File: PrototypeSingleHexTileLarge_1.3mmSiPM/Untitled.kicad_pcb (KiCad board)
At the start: 2 copper layers, 44.6 x 38.6 mm, 7 parts

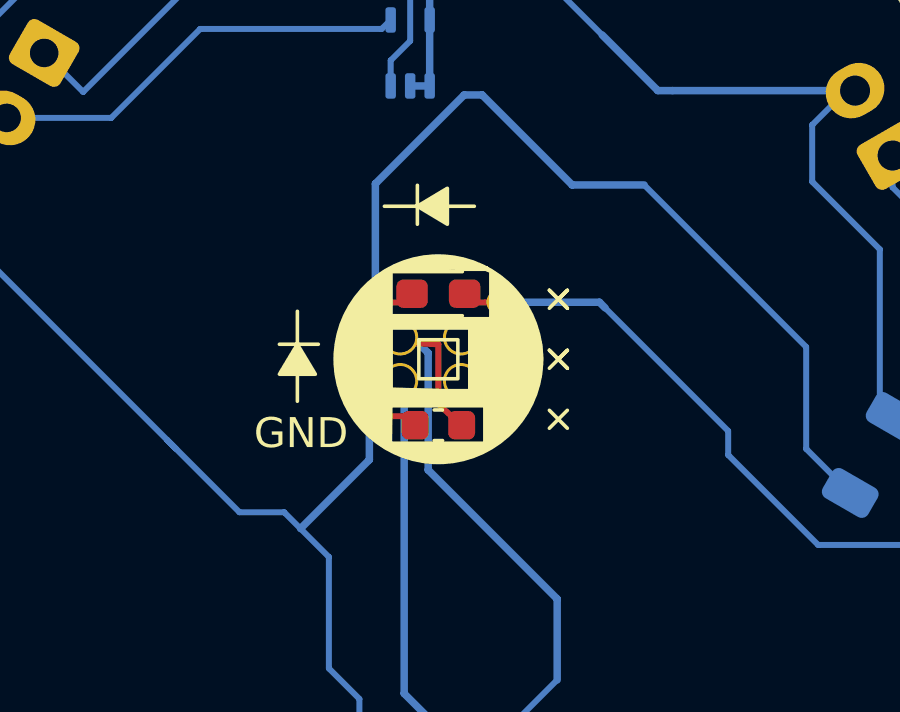
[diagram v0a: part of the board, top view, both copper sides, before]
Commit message: updated 1.3 mm SiPM board (single hex).  Increased size of holes for the pogos
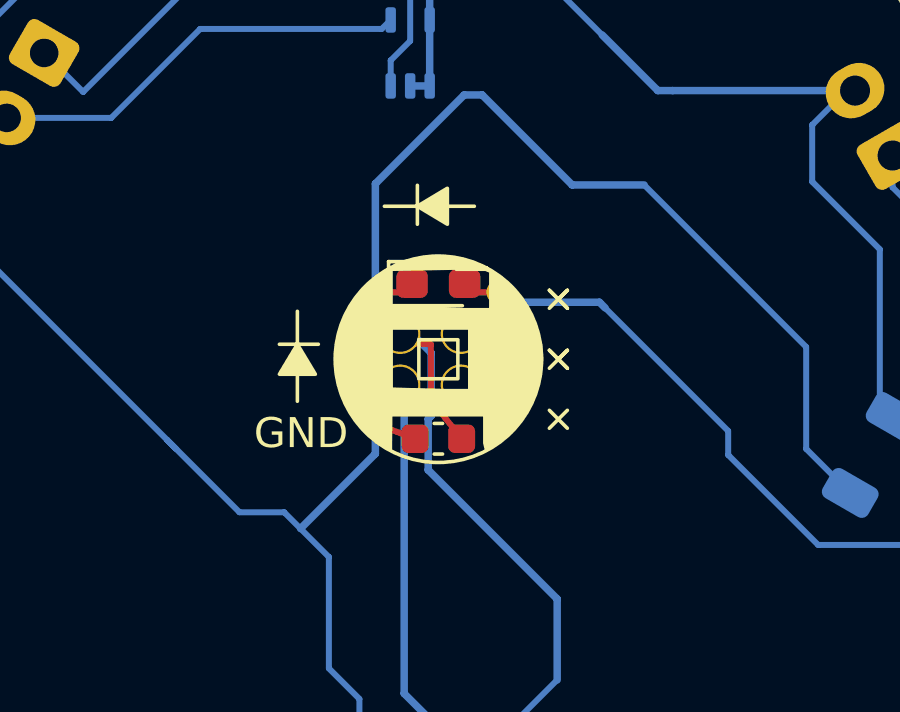
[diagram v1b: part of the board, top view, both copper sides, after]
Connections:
- REF** pad 5: (no net) -> LED_C
- REF** pad 6: (no net) -> LED_A
- REF** pad 7: (no net) -> SiPM_C
- REF** pad 8: (no net) -> SiPM_A
- REF** pad 9: (no net) -> GND
- REF** pad 1: (no net) -> GND (x2)
- REF** pad 2: (no net) -> GND (x2)
- REF** pad 3: (no net) -> TMP_OUT
- REF** pad 4: (no net) -> TMP_VDD
- REF** pad 5: (no net) -> GND
- REF** pad 1: (no net) -> TMP_OUT
- REF** pad 2: (no net) -> TMP_VDD
- REF** pad 3: (no net) -> GND (x2)
- REF** pad 1: (no net) -> SiPM_C
- REF** pad 2: (no net) -> SiPM_A
- REF** pad 2: (no net) -> LED_C
- REF** pad 1: (no net) -> LED_A
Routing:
- net (no net): track 224.4 -> 0.00 mm
- net GND: track 0.00 -> 90.2 mm
- net LED_A: track 0.00 -> 33.4 mm
- net LED_C: track 0.00 -> 28.2 mm
- net SiPM_C: track 0.00 -> 21.1 mm
- net TMP_OUT: track 0.00 -> 19.2 mm
- net SiPM_A: track 0.00 -> 17.0 mm
- net TMP_VDD: track 0.00 -> 15.1 mm
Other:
- board text added: "Designed by Sebouh J. Paul v4. 1.3 mm SiPM sidelength=22.30 mm"
- board text removed: "Designed by Sebouh J. Paul v3. 1.3 mm SiPM sidelength=22.30 mm"
